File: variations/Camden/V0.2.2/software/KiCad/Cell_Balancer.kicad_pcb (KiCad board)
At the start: 2 copper layers, 12 parts, among them J1 Screw_Terminal_01x11, J2 DC37_Pins

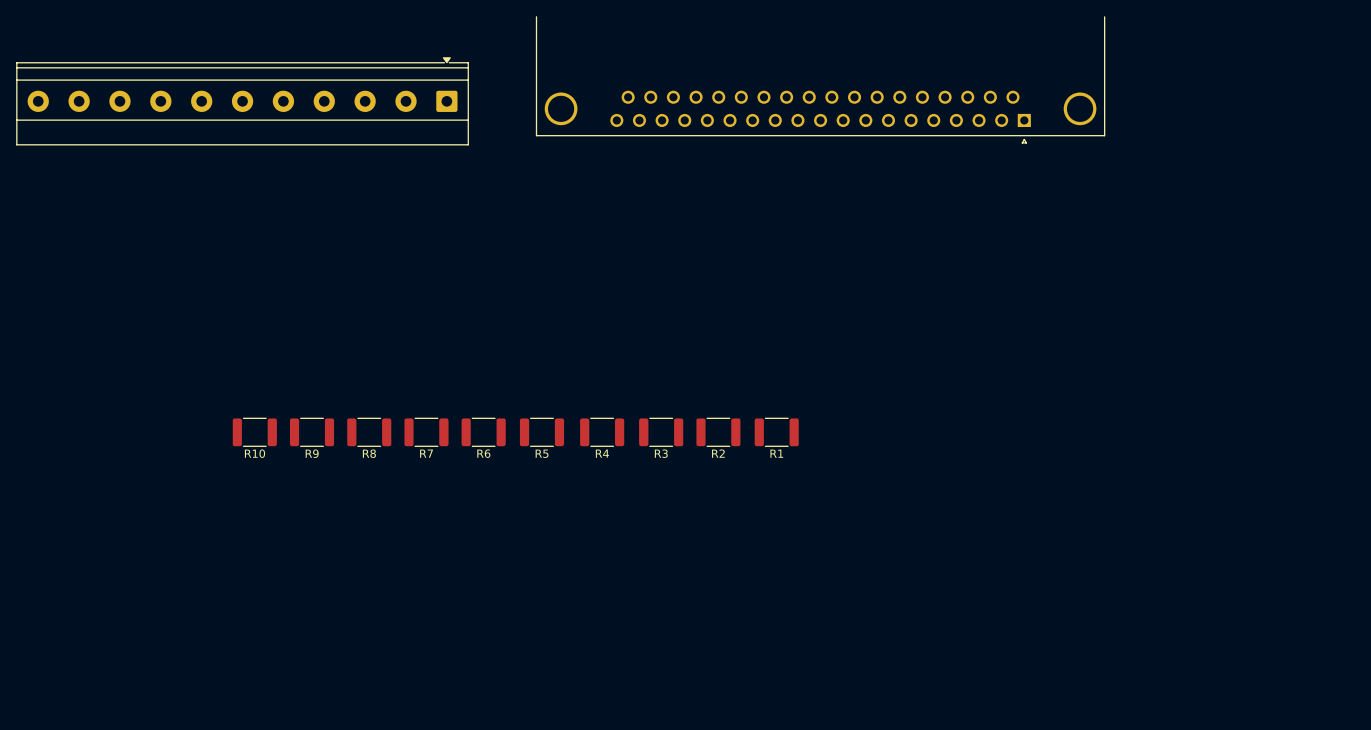
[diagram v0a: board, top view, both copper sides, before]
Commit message: KiCAD update
figured out the issue with the pcb copper tracks, software crashed a couple of times so there are a lot of autosaves, next step is getting the mounting holes the right size and correct distance then it will be ready to go
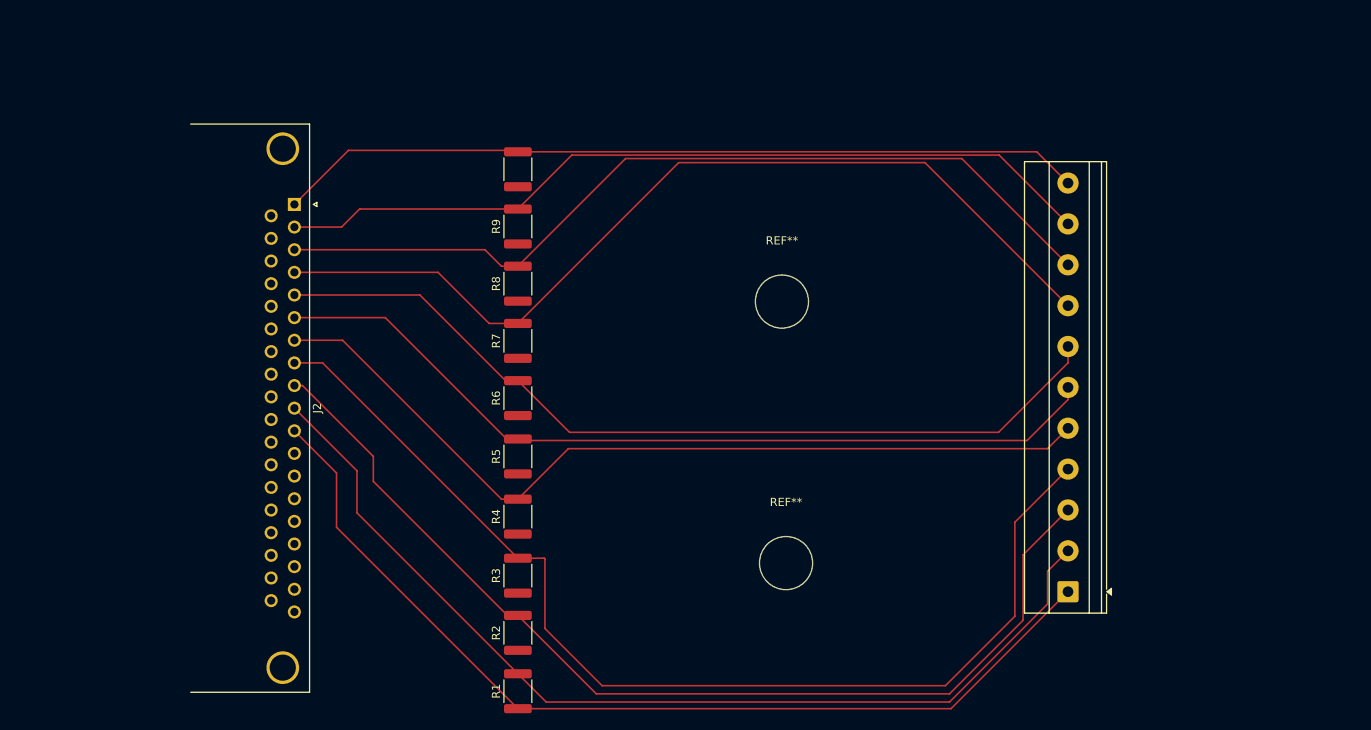
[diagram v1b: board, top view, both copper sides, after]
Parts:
- added REF**: MountingHole_6.5mm, MountingHole:MountingHole_6.5mm, F.Cu at (132.0, 100.0)
- added REF**: MountingHole_6.5mm, MountingHole:MountingHole_6.5mm, F.Cu at (132.5, 132.0)
- moved J1 96.8 mm to (167.0, 135.5), turned to 90 degrees
- moved J2 89.9 mm to (72.3, 88.1), turned to -90 degrees
- moved R10 45.5 mm to (99.7, 83.8), turned to 90 degrees
- moved R1 44.8 mm to (99.7, 147.7), turned to 90 degrees
- moved R9 35.6 mm to (99.7, 90.8), turned to 90 degrees
- moved R2 34.7 mm to (99.7, 140.5), turned to 90 degrees
- moved R8 25.7 mm to (99.7, 97.8), turned to 90 degrees
- moved R3 24.8 mm to (99.7, 133.5), turned to 90 degrees
- moved R7 15.8 mm to (99.7, 104.8), turned to 90 degrees
- moved R4 14.6 mm to (99.7, 126.3), turned to 90 degrees
- moved R6 5.92 mm to (99.7, 111.8), turned to 90 degrees
- moved R5 4.17 mm to (99.7, 119.0), turned to 90 degrees
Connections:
- J2 pad 1: Net-(J1-Pin_1) -> Net-(J1-Pin_11)
- J2 pad 10: Net-(J1-Pin_10) -> Net-(J1-Pin_2)
- J2 pad 11: Net-(J1-Pin_11) -> Net-(J1-Pin_1)
- J2 pad 2: Net-(J1-Pin_2) -> Net-(J1-Pin_10)
- J2 pad 3: Net-(J1-Pin_3) -> Net-(J1-Pin_9)
- J2 pad 4: Net-(J1-Pin_4) -> Net-(J1-Pin_8)
- J2 pad 5: Net-(J1-Pin_5) -> Net-(J1-Pin_7)
- J2 pad 7: Net-(J1-Pin_7) -> Net-(J1-Pin_5)
- J2 pad 8: Net-(J1-Pin_8) -> Net-(J1-Pin_4)
- J2 pad 9: Net-(J1-Pin_9) -> Net-(J1-Pin_3)
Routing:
- net Net-(J1-Pin_4): track 0.00 -> 133.7 mm
- net Net-(J1-Pin_3): track 0.00 -> 126.1 mm
- net Net-(J1-Pin_2): track 0.00 -> 122.6 mm
- net Net-(J1-Pin_1): track 0.00 -> 118.6 mm
- net Net-(J1-Pin_8): track 0.00 -> 112.6 mm
- net Net-(J1-Pin_7): track 0.00 -> 107.1 mm
- net Net-(J1-Pin_9): track 0.00 -> 106.3 mm
- net Net-(J1-Pin_5): track 0.00 -> 106.3 mm
- net Net-(J1-Pin_6): track 0.00 -> 104.5 mm
- net Net-(J1-Pin_10): track 0.00 -> 101.8 mm
- net Net-(J1-Pin_11): track 0.00 -> 99.1 mm

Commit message: update
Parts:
- moved R1 31.7 mm to (124.5, 128.0), turned to 0 degrees
- moved R2 30.4 mm to (124.5, 123.0), turned to 180 degrees
- moved J1 29.5 mm to (196.5, 134.5)
- moved REF** 29.5 mm to (161.5, 99.0)
- moved REF** 29.5 mm to (162.0, 131.0)
- moved R3 29.3 mm to (124.5, 118.0), turned to 180 degrees
- moved R4 28.2 mm to (124.5, 113.0), turned to 180 degrees
- moved R5 27.1 mm to (124.5, 108.0), turned to 180 degrees
- moved R6 26.3 mm to (124.5, 103.0), turned to 180 degrees
- moved R7 25.7 mm to (124.5, 98.0), turned to 180 degrees
- moved R8 25.3 mm to (124.5, 93.0), turned to 180 degrees
- moved J2 25.0 mm to (97.3, 87.6)
- moved R9 25.0 mm to (124.5, 88.0), turned to 180 degrees
- moved R10 24.8 mm to (124.5, 83.0), turned to 180 degrees
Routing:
- net Net-(J1-Pin_4): track 133.7 -> 108.9 mm
- net Net-(J1-Pin_6): track 104.5 -> 110.0 mm
- net Net-(J1-Pin_11): track 99.1 -> 104.2 mm
- net Net-(J1-Pin_7): track 107.1 -> 111.9 mm
- net Net-(J1-Pin_10): track 101.8 -> 106.6 mm
- net Net-(J1-Pin_9): track 106.3 -> 108.5 mm
- net Net-(J1-Pin_5): track 106.3 -> 108.0 mm
- net Net-(J1-Pin_1): track 118.6 -> 117.1 mm
- net Net-(J1-Pin_2): track 122.6 -> 124.0 mm
- net Net-(J1-Pin_3): track 126.1 -> 125.2 mm
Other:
- board outline added: 118 x 75 mm

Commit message: update
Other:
- board text added: "Cebastione Bailey Cell Balancer V.2.20 ARTS-Lab 9-1-2026"
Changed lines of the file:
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@@
 		(layer "Edge.Cuts")
+	)
+	(gr_text "Cebastione Bailey\nCell Balancer V.2.20\nARTS-Lab\n9-1-2026\n"
+		(at 100.5 136.5 0)
+		(layer "Edge.Cuts")
+		(effects
+			(font
+				(size 1 1)
+				(thickness 0.15)
+			)
+			(justify left bottom)
+		)
 	)
 	(segment
